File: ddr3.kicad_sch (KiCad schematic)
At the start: 8 parts, among them U8 MT41K256M16TW-107:P

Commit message: wip rickard
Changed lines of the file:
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@@
 		(polyline
 			(pts
-				(xy 82.55 116.84) (xy 82.55 129.54) (xy 87.63 129.54) (xy 87.63 116.84)
+				(xy 137.16 69.85) (xy 137.16 88.9) (xy 144.78 88.9) (xy 144.78 69.85)
 			)
 			(stroke
@@
 			(fill
 				(type none)
+			)
+		)
+	)
+	(rule_area
+		(polyline
+			(pts
+				(xy 82.55 116.84) (xy 82.55 129.54) (xy 87.63 129.54) (xy 87.63 116.84)
+			)
+			(stroke
+				(width 0)
+				(type dash)
+			)
+			(fill
+				(type none)
+			)
+		)
+	)
+	(rule_area
+		(polyline
+			(pts
+				(xy 137.16 45.72) (xy 137.16 67.31) (xy 144.78 67.31) (xy 144.78 45.72)
+			)
+			(stroke
+				(width 0)
+				(type dash)
+			)
+			(fill
+				(type none)
+			)
+		)
+	)
+	(netclass_flag ""
+		(length 2.54)
+		(shape round)
+		(at 139.7 45.72 0)
+		(fields_autoplaced yes)
+		(effects
+			(font
+				(size 1.27 1.27)
+			)
+			(justify left bottom)
+		)
+		(property "Netclass" "DDR3_DQ_LO"
+			(at 140.3985 43.18 0)
+			(effects
+				(font
+					(size 1.27 1.27)
+				)
+				(justify left)
+			)
+		)
+		(property "Component Class" ""
+			(at -27.94 16.51 0)
+			(effects
+				(font
+					(size 1.27 1.27)
+					(italic yes)
+				)
+			)
+		)
+	)
+	(netclass_flag ""
+		(length 2.54)
+		(shape round)
+		(at 144.78 88.9 180)
+		(fields_autoplaced yes)
+		(effects
+			(font
+				(size 1.27 1.27)
+			)
+			(justify right bottom)
+		)
+		(property "Netclass" "DDR3_DQ_HI"
+			(at 145.4785 91.44 0)
+			(effects
+				(font
+					(size 1.27 1.27)
+				)
+				(justify left)
+			)
+		)
+		(property "Component Class" ""
+			(at -22.86 59.69 0)
+			(effects
+				(font
+					(size 1.27 1.27)
+					(italic yes)
+				)
 			)
 		)
@@
 		)
 		(property "Value" "240"
-			(at 76.2 154.9399 0)
+			(at 80.01 154.432 0)
 			(effects
 				(font

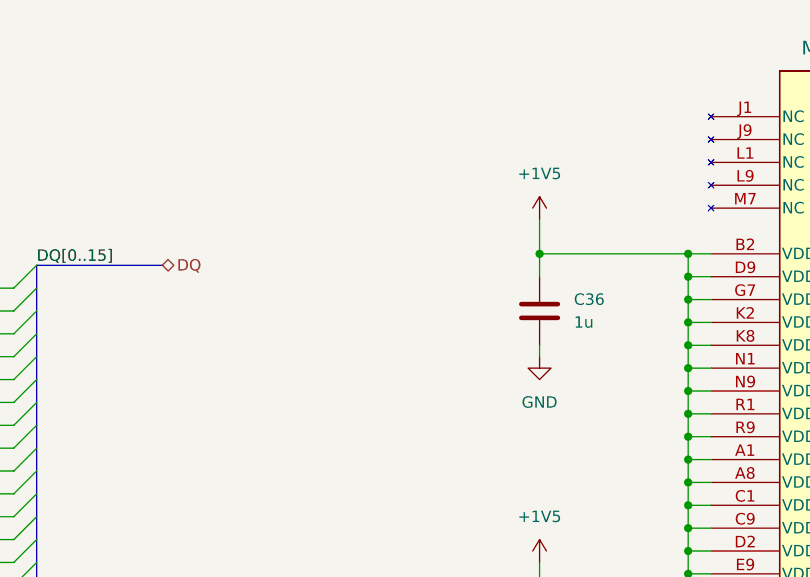
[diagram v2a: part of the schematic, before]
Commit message: changed ddr3 pinning according to hard-ip in vivado
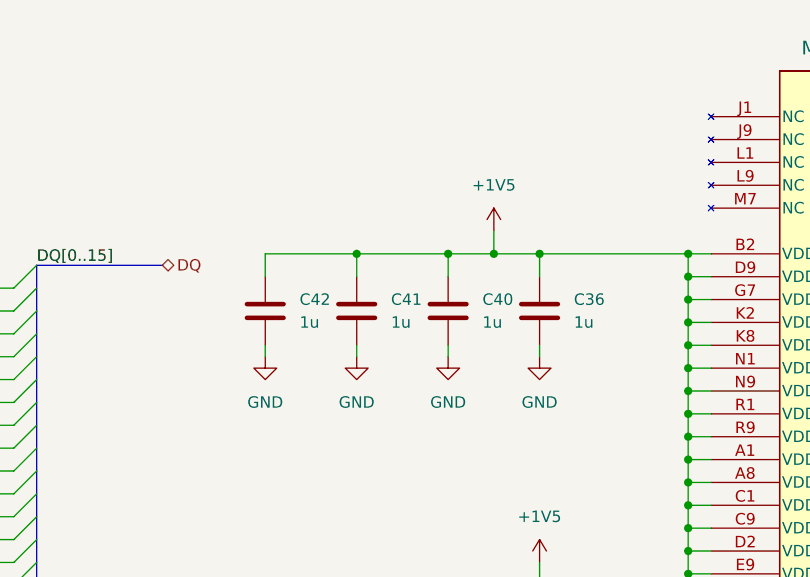
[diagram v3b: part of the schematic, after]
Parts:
- added C40, C41, C42: 1u, Capacitor_SMD:C_0402_1005Metric, symbol Device:C
- R18, R19, R20: footprint (none) -> Resistor_SMD:R_0402_1005Metric
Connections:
- net +1V5: now also C40.1, C41.1, C42.1
- net GND: now also C40.2, C41.2, C42.2
